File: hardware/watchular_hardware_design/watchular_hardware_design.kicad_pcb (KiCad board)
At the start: 4 copper layers, 55.5 x 22.9 mm, 89 parts, among them J1 USB4105-GF-A, J2 665102131822, J3 TSW-116-07-H-S, J4 TSW-116-07-H-S, Q1 BSS123, Q2 BSS123, Q3 BSS123, Q4 BSS123, T1 DMG1013UW-7, U1 MCP73832T-2DCI/OT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

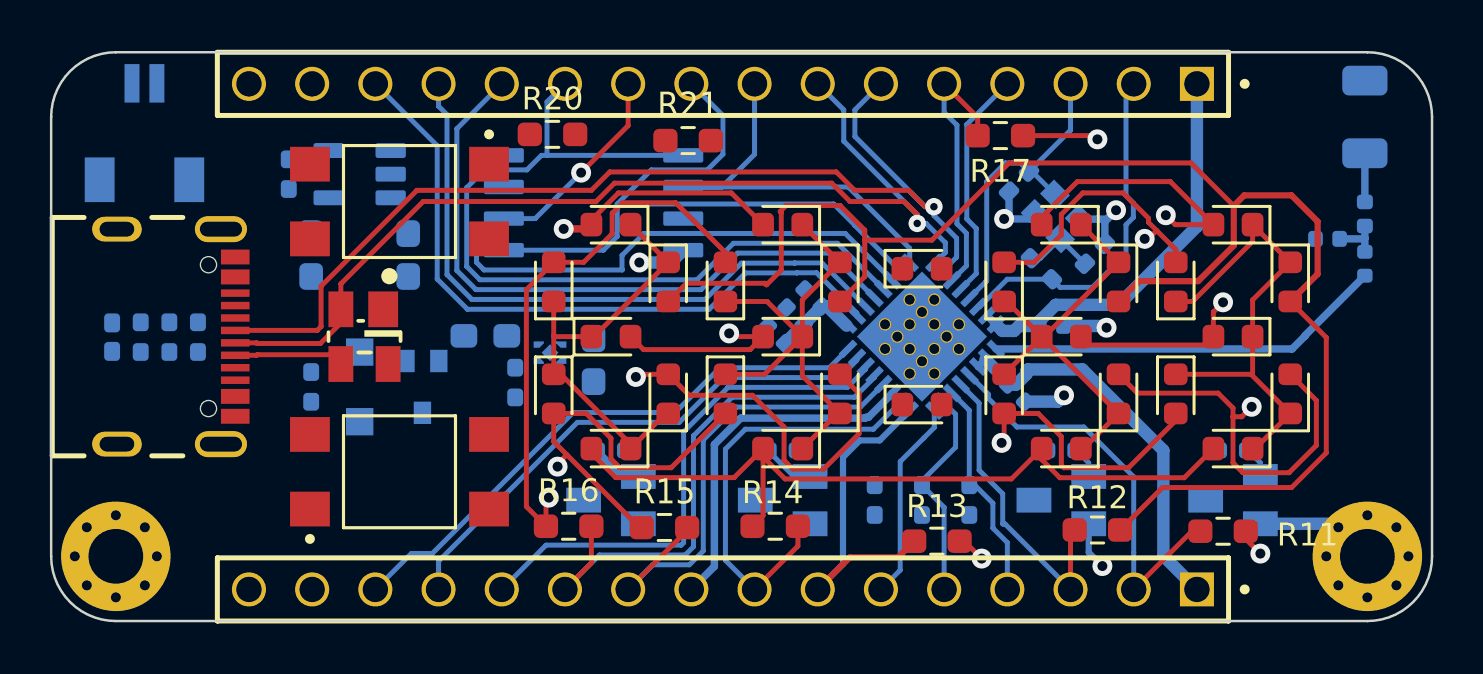
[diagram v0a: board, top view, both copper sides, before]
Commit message: Drivers for right two digits wired in.
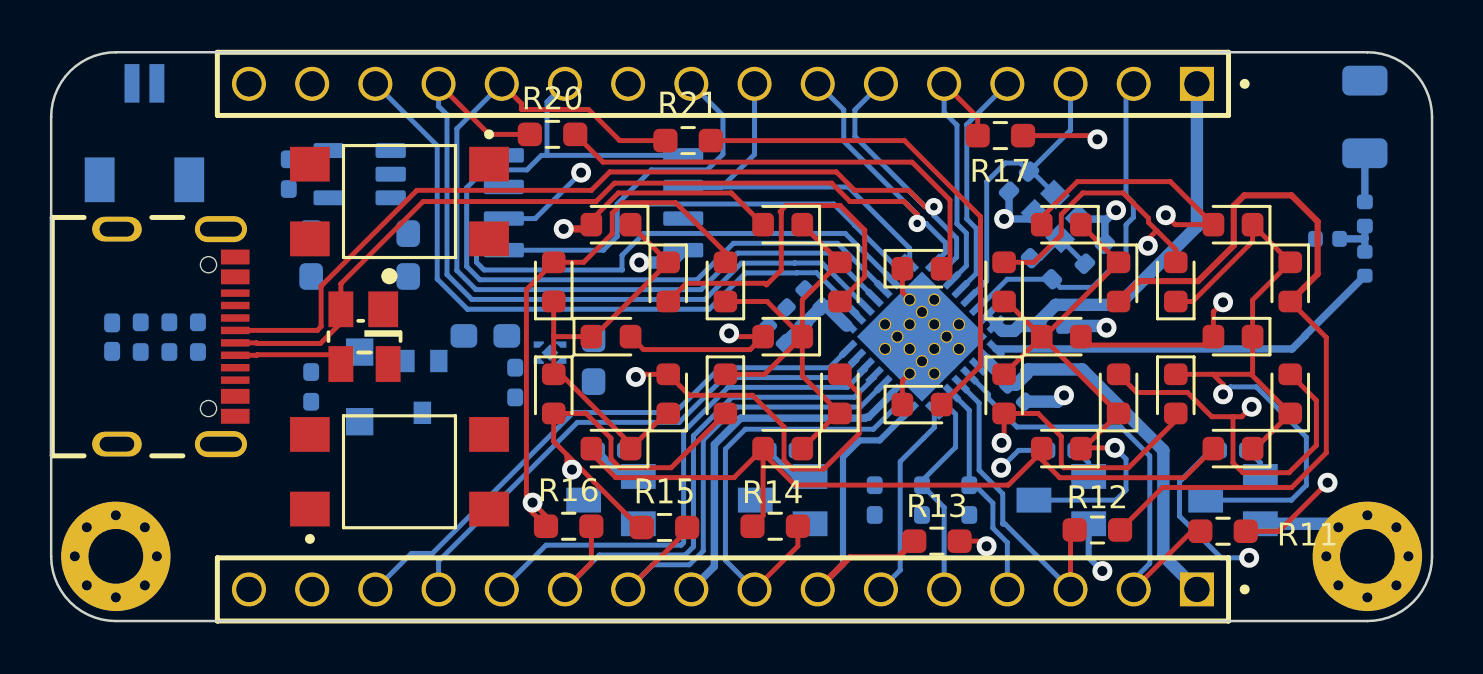
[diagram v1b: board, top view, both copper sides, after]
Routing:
- net DIGI3_STRAP: track 21.4 -> 62.0 mm, vias 0 -> 1
- net DIGI2: track 23.0 -> 52.4 mm, vias 0 -> 1
- net Net-(D18-Pad2): track 0.00 -> 20.3 mm
- net Net-(D17-Pad2): track 0.00 -> 19.1 mm
- net G: track 64.6 -> 47.7 mm
- net B: track 62.7 -> 45.9 mm
- net Net-(D26-Pad1): track 20.1 -> 31.7 mm, vias 0 -> 1
- net A: track 61.6 -> 71.1 mm
- net DIV1-with_no_internal_flash_ONLY: track 26.7 -> 34.4 mm
- net Net-(D19-Pad1): track 17.6 -> 24.7 mm, vias 0 -> 1
- net C: track 69.9 -> 64.1 mm
- net DIV0-with_no_internal_flash_ONLY: track 26.4 -> 30.9 mm
- net E: track 48.8 -> 44.5 mm
- net GND: track 17.9 -> 20.8 mm
- net A_MCU: track 16.6 -> 18.0 mm
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- added copper zone on In1.Cu, net VDD3P3
- removed copper zone on In1.Cu, net GND

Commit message: Added pour zones to all the layers.
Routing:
- added copper zone on B.Cu, net GND
- added copper zone on F.Cu, net GND
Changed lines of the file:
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@@
   (segment (start 119.875 118.475) (end 117.742228 118.475) (width 0.2) (layer "B.Cu") (net 60))
   (segment (start 117.742228 118.475) (end 116.282228 119.935) (width 0.2) (layer "B.Cu") (net 60))
+  (zone (net 3) (net_name "GND") (layer "F.Cu") (hatch edge 0.508)
+    (connect_pads (clearance 0))
+    (min_thickness 0.25) (filled_areas_thickness no)
+    (fill yes (thermal_gap 0.5) (thermal_bridge_width 0.5))
+    (polygon
+      (pts
+        (xy 137.55 116.5)
+        (xy 145.5 116.5)
+        (xy 145.5 133)
+        (xy 90 133)
+        (xy 90 110)
+        (xy 137.55 110)
+      )
+    )
+  )
   (zone (net 43) (net_name "VDD3P3") (layer "In1.Cu") (hatch edge 0.508)
     (connect_pads (clearance 0))
@@
         (xy 90 133)
         (xy 90 110)
+        (xy 137.5 110)
+      )
+    )
+  )
+  (zone (net 3) (net_name "GND") (layer "B.Cu") (hatch edge 0.508)
+    (connect_pads (clearance 0))
+    (min_thickness 0.25) (filled_areas_thickness no)
+    (fill yes (thermal_gap 0.5) (thermal_bridge_width 0.5))
+    (polygon
+      (pts
+        (xy 137.5 116.5)
+        (xy 145.5 116.5)
+        (xy 145.5 133)
+        (xy 90 133)
+        (xy 90 110)

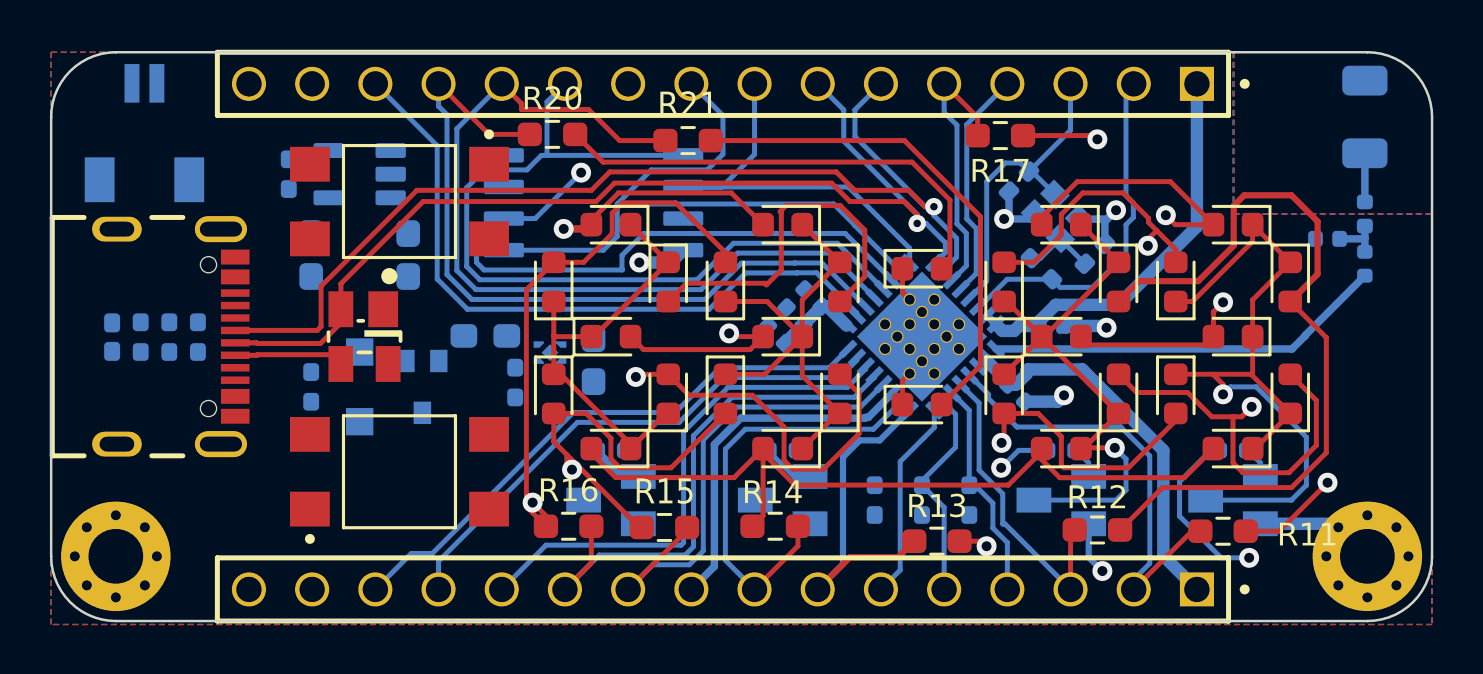
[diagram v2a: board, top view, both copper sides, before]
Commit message: All the digits connected.
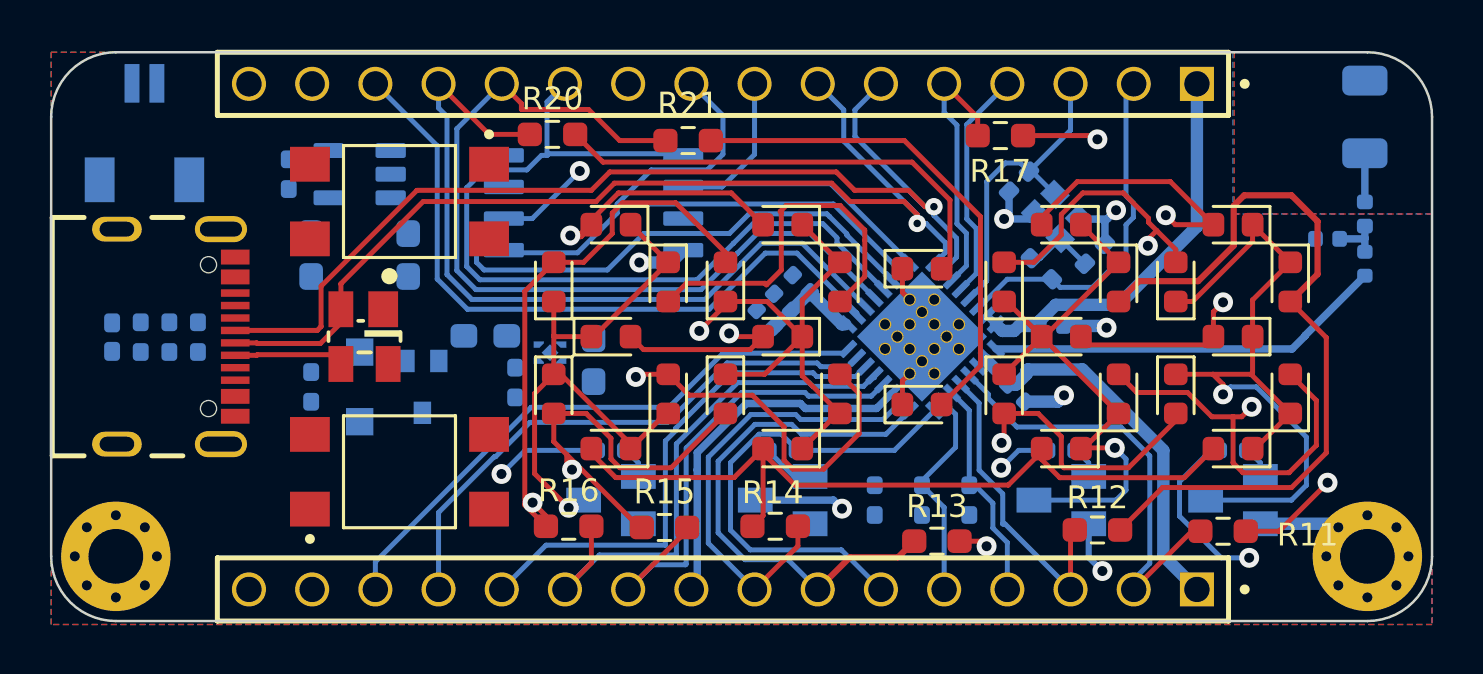
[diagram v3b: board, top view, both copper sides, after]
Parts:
- moved C10 0.79 mm to (118.7, 120.7)
- moved C7 0.75 mm to (120.2, 119.3)
- moved C8 0.74 mm to (119.4, 120.0)
- turned R18 to 0 degrees
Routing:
- net DIGI0: track 9.34 -> 45.2 mm, vias 0 -> 1
- net Net-(D10-Pad1): track 19.1 -> 46.2 mm, vias 0 -> 2
- net DIGI1: track 8.08 -> 19.3 mm
- net C_MCU: track 13.9 -> 21.4 mm
- net Net-(D3-Pad1): track 17.4 -> 24.4 mm, vias 0 -> 1
- net DIGI3_STRAP: track 62.0 -> 63.2 mm
- net D_MCU: track 17.2 -> 18.2 mm
- net VDD3P3: track 50.0 -> 50.9 mm
- net Net-(Q1-Pad1): track 2.28 -> 1.41 mm
- net CS-memory: track 34.0 -> 34.8 mm
- net GPIO11-to_breakout-TEST_ONLY: track 27.6 -> 28.3 mm
- net DIV0-with_no_internal_flash_ONLY: track 30.9 -> 31.5 mm
- net DIV1-with_no_internal_flash_ONLY: track 34.4 -> 35.0 mm
- net DIGI2: track 52.4 -> 53.0 mm

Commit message: Buttons wired in.
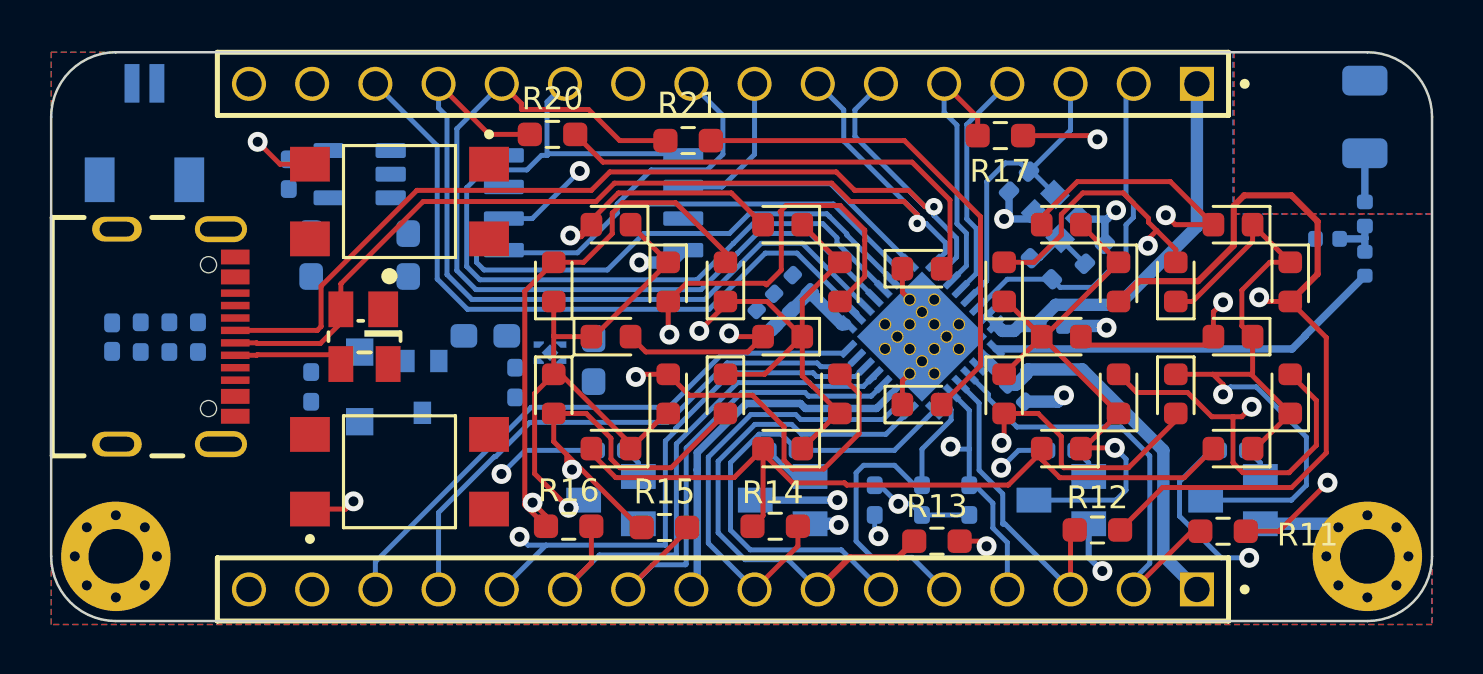
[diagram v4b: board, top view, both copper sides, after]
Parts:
- turned R8 to 90 degrees
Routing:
- net BUTTON1_STRAP: track 21.0 -> 60.9 mm, vias 0 -> 3
- net B: track 45.9 -> 75.9 mm, vias 0 -> 2
- net BUTTON0_STRAP: track 8.95 -> 36.5 mm, vias 0 -> 2
- net VDD3P3: track 50.9 -> 65.0 mm, vias 0 -> 1
- net CHIP_EN: track 8.68 -> 14.2 mm
- net GND: track 20.8 -> 22.0 mm, vias 6 -> 7
- net Net-(D26-Pad1): track 31.7 -> 32.5 mm
- added copper zone on In2.Cu, net GND
- removed copper zone on In2.Cu, net VDD3P3

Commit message: Aligned the resistors on the front side.
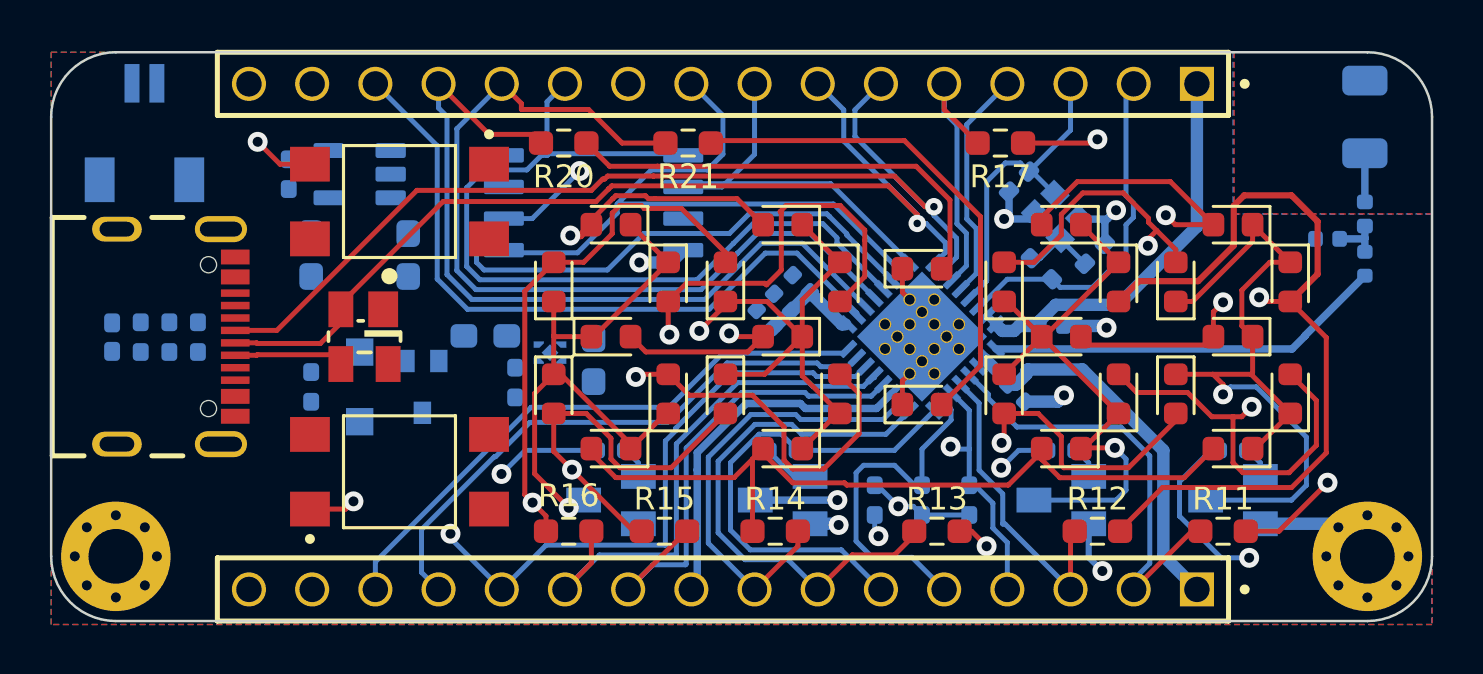
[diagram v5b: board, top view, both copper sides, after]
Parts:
- moved R20 0.57 mm to (110.6, 113.7)
- moved R13 0.40 mm to (125.6, 129.2)
- moved R17 0.30 mm to (128.2, 113.7)
- moved R14 0.20 mm to (119.1, 129.2)
- moved R16 0.20 mm to (110.8, 129.2)
- moved R15 0.15 mm to (114.7, 129.2)
- moved R21 0.10 mm to (115.6, 113.7)
- moved R12 0.05 mm to (132.1, 129.2)
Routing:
- net BUTTON1_STRAP: track 60.9 -> 63.4 mm
- net USB_D+: track 46.8 -> 45.7 mm
- net F: track 66.2 -> 65.2 mm
- net DIV0-with_no_internal_flash_ONLY: track 31.5 -> 32.1 mm
- net Net-(D17-Pad2): track 19.1 -> 18.5 mm
- net DIGI3_STRAP: track 63.2 -> 63.8 mm
- net USB_D-: track 42.5 -> 41.9 mm

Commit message: Started wiring the power part.
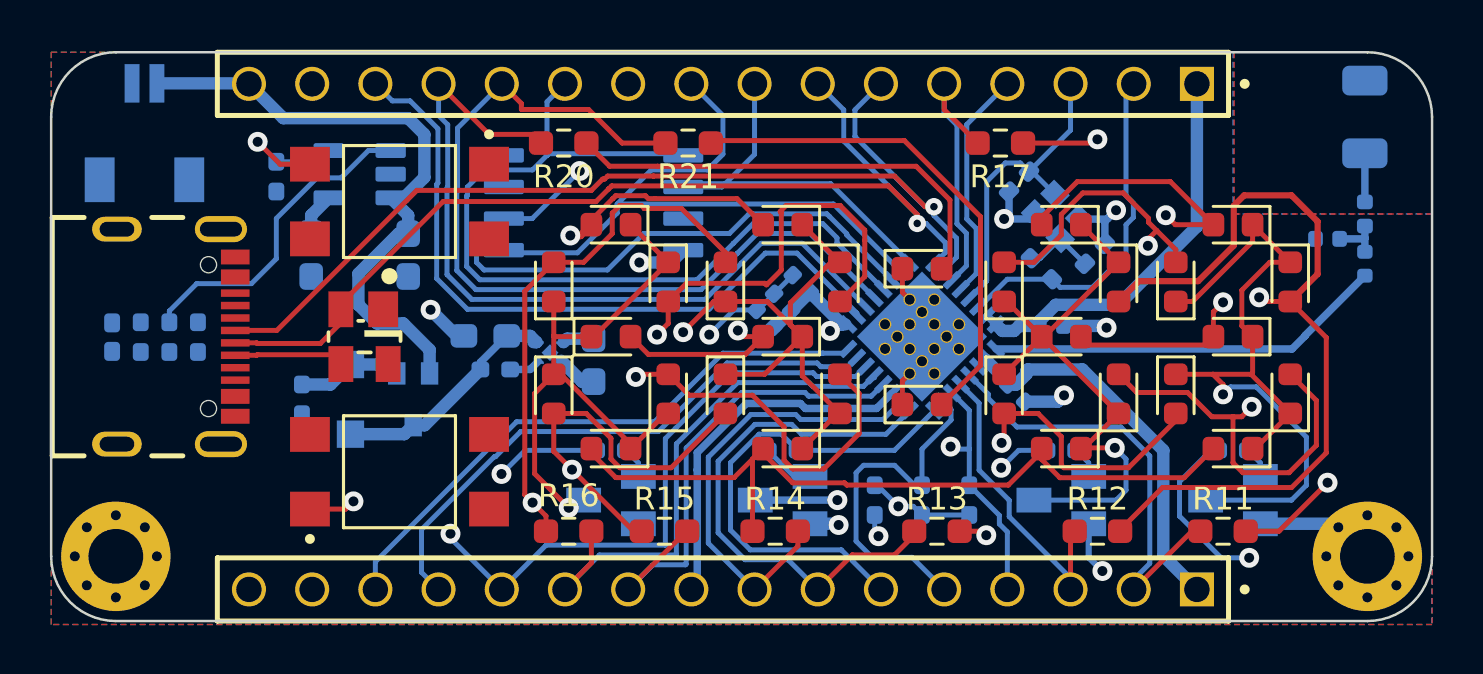
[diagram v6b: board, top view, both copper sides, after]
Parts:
- moved R7 0.96 mm to (107.8, 122.8), turned to 0 degrees
- moved D1 0.62 mm to (102.0, 124.0)
- moved R6 0.62 mm to (100.1, 124.0)
- moved T1 0.62 mm to (104.5, 124.0)
- moved R4 0.51 mm to (99.0, 115.0)
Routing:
- net +BATT: track 0.00 -> 25.2 mm
- net VDD3P3: track 64.9 -> 80.2 mm, vias 1 -> 2
- net BATT_STAT: track 0.00 -> 13.0 mm
- net VCC: track 0.00 -> 9.50 mm
- net GND: track 22.0 -> 30.3 mm, vias 7 -> 9
- net +5V: track 0.00 -> 6.02 mm
- net Net-(R4-Pad1): track 0.00 -> 2.29 mm
- net Net-(R7-Pad2): track 0.00 -> 1.26 mm
- net B: track 76.0 -> 76.6 mm
- net Net-(D10-Pad1): track 46.1 -> 46.7 mm
- net C: track 64.3 -> 63.6 mm
- net G: track 48.3 -> 47.6 mm

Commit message: Added 5V pouring area.
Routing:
- added copper zone on In1.Cu, net +5V
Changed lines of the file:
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@@
         (xy 145.5 116.5)
         (xy 145.5 133)
-        (xy 90 133)
-        (xy 90 110)
+        (xy 105.25 133)
+        (xy 105.25 110)
         (xy 137.5 110)
       )
     )
+  )
+  (zone (net 21) (net_name "+5V") (layer "In1.Cu") (hatch edge 0.508)
+    (connect_pads (clearance 0.3))
+    (min_thickness 0.25) (filled_areas_thickness no)
+    (fill yes (thermal_gap 0.5) (thermal_bridge_width 0.5))
+    (polygon
+      (pts
+        (xy 105.15 133)
+        (xy 90 133)
+        (xy 90 110)
+        (xy 105.15 110)
+      )
+    )

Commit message: Everything connected.
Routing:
- net +5V: track 6.02 -> 16.5 mm, vias 0 -> 4
- net BUTTON1_STRAP: track 63.9 -> 71.1 mm
- net VDD3P3: track 80.2 -> 87.3 mm, vias 2 -> 6
- net BUTTON0_STRAP: track 36.4 -> 42.9 mm
- net Net-(D2-Pad1): track 0.00 -> 5.46 mm
- net Net-(J1-PadB5): track 0.00 -> 4.88 mm, vias 0 -> 1
- net GND: track 30.3 -> 33.4 mm, vias 9 -> 11
- net Net-(J1-PadA5): track 0.00 -> 2.41 mm, vias 0 -> 1
- net F: track 65.2 -> 63.6 mm
- net DIV1-with_no_internal_flash_ONLY: track 35.1 -> 36.5 mm
- net GPIO11-to_breakout-TEST_ONLY: track 28.7 -> 29.9 mm
- net DIGI0: track 45.2 -> 46.3 mm
- net Net-(D10-Pad1): track 46.7 -> 47.8 mm
- net DIV0-with_no_internal_flash_ONLY: track 32.2 -> 33.2 mm
- net C: track 63.6 -> 62.7 mm
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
